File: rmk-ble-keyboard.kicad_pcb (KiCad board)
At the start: 2 copper layers, 285 x 94.5 mm, 124 parts, among them SW1 esc, SW10 9, SW11 0, SW12 -, SW13 =, SW14 backspace, SW15 tab, SW16 q, SW17 w, SW18 e, SW19 r, SW2 1, SW20 t, SW21 y, SW22 u, SW23 i, SW24 o, SW25 p, SW26 [, SW27 ], SW28 \, SW29 capslock, SW3 2, SW30 a, SW31 s, SW32 d, SW33 f, SW34 g, SW35 h, SW36 j, SW37 k, SW38 l, SW39 ;, SW4 3, SW40 ', SW41 enter, SW42 lshift, SW43 z, SW44 x, SW45 c, SW46 v, SW47 b, SW48 n, SW49 m, SW5 4, SW50 ,, SW51 ., SW52 /, SW53 rshift, SW54 lctrl, SW55 lgui, SW56 lalt, SW57 space, SW58 ralt, SW59 rgui, SW6 5, SW60 fn, SW61 rctrl, SW7 6, SW8 7, SW9 8, U2 USBLC6-2SC6

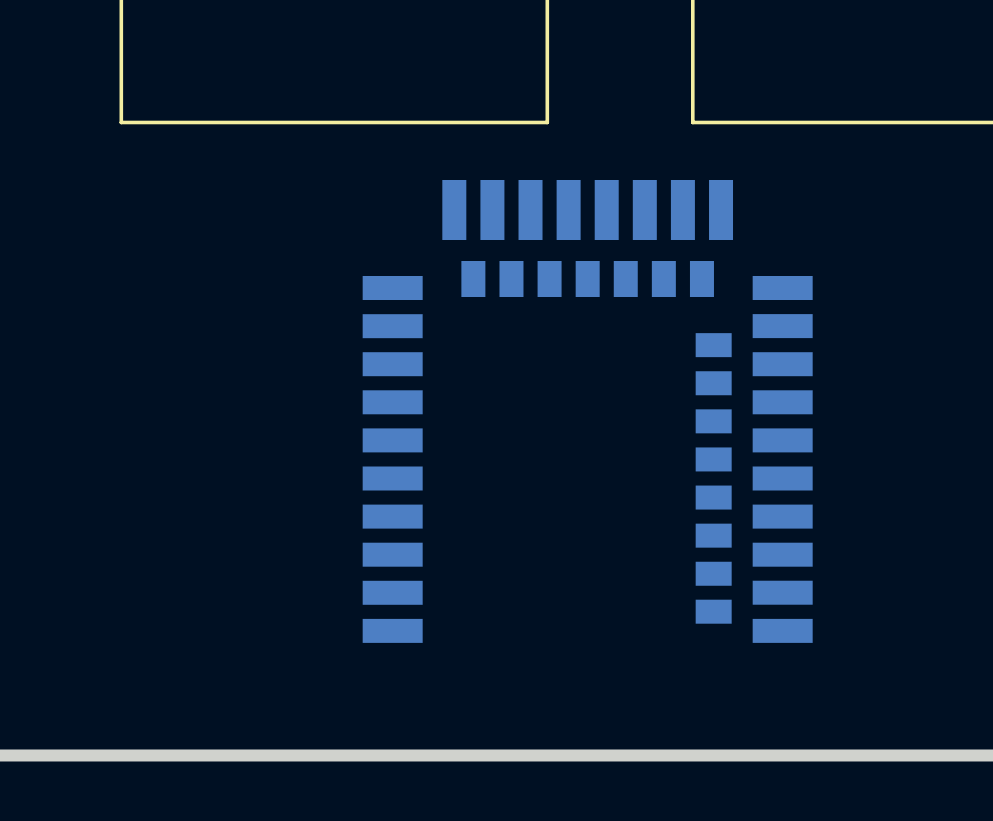
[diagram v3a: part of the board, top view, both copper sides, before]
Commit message: schema: rev0 done
Signed-off-by: HaoboGu <haobogu@outlook.com>
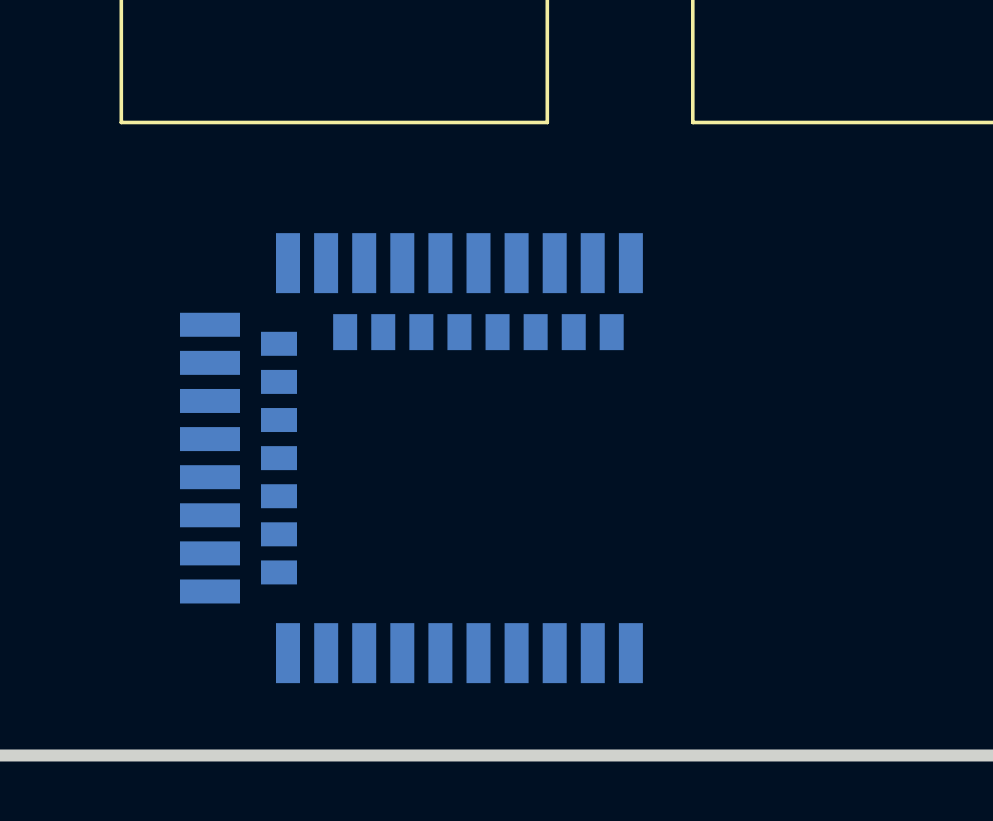
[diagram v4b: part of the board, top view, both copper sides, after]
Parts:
- moved U1 19.2 mm to (114.9, 107.0), turned to 0 degrees
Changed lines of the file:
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@@
 	(footprint "E73_2G4M08S1C:E73(2G4M08S1C)"
 		(layer "B.Cu")
-		(at 134.008 105.267 -90)
+		(at 114.919 107.038)
 		(property "Reference" "U1"
-			(at 8.525 14.7003 90)
+			(at 8.525 14.7003 180)
 			(unlocked yes)
 			(layer "B.SilkS")
@@
 		)
 		(property "Value" "~"
-			(at 8.525 -1.7003 90)
+			(at 8.525 -1.7003 180)
 			(unlocked yes)
 			(layer "B.Fab")
@@
 		)
 		(property "Footprint" "E73_2G4M08S1C:E73(2G4M08S1C)"
-			(at 0 0 90)
+			(at 0 0 180)
 			(unlocked yes)
 			(layer "B.Fab")
@@
 		)
 		(property "Datasheet" ""
-			(at 0 0 90)
+			(at 0 0 180)
 			(unlocked yes)
 			(layer "B.Fab")
@@
 		)
 		(property "Description" ""
-			(at 0 0 90)
+			(at 0 0 180)
 			(unlocked yes)
 			(layer "B.Fab")
@@
 		)
 		(fp_line
+			(start 18 0)
+			(end 0 0)
+			(stroke
+				(width 0.1)
+				(type solid)
+			)
+			(layer "B.SilkS")
+		)
+		(fp_line
 			(start 18 13)
 			(end 0 13)
@@
 			(layer "B.SilkS")
 		)
-		(fp_line
-			(start 18 0)
-			(end 0 0)
-			(stroke
-				(width 0.1)
-				(type solid)
-			)
-			(layer "B.SilkS")
-		)
 		(pad "1" smd rect
-			(at 14.03 13)
+			(at 14.03 13 90)
 			(size 2 0.8)
 			(layers "B.Cu" "B.Paste" "B.Mask")
@@
 		)
 		(pad "2" smd rect
-			(at 12.76 13)
+			(at 12.76 13 90)
 			(size 2 0.8)
 			(layers "B.Cu" "B.Paste" "B.Mask")
@@
 		)
 		(pad "3" smd rect
-			(at 11.49 13)
+			(at 11.49 13 90)
 			(size 2 0.8)
 			(layers "B.Cu" "B.Paste" "B.Mask")
@@
 		)
 		(pad "4" smd rect
-			(at 10.22 13)
+			(at 10.22 13 90)
 			(size 2 0.8)
 			(layers "B.Cu" "B.Paste" "B.Mask")
@@
 		)
 		(pad "5" smd rect
-			(at 8.95 13)
+			(at 8.95 13 90)
 			(size 2 0.8)
 			(layers "B.Cu" "B.Paste" "B.Mask")
@@
 		)
 		(pad "6" smd rect
-			(at 7.68 13)
+			(at 7.68 13 90)
 			(size 2 0.8)
 			(layers "B.Cu" "B.Paste" "B.Mask")
@@
 		)
 		(pad "7" smd rect
-			(at 6.41 13)
+			(at 6.41 13 90)
 			(size 2 0.8)
 			(layers "B.Cu" "B.Paste" "B.Mask")
@@
 		)
 		(pad "8" smd rect
-			(at 5.14 13)
+			(at 5.14 13 90)
 			(size 2 0.8)
 			(layers "B.Cu" "B.Paste" "B.Mask")
@@
 		)
 		(pad "9" smd rect
-			(at 3.8728 13.0003)
+			(at 3.8728 13.0003 90)
 			(size 2 0.8)
 			(layers "B.Cu" "B.Paste" "B.Mask")
@@
 		)
 		(pad "10" smd rect
-			(at 2.6 13)
+			(at 2.6 13 90)
 			(size 2 0.8)
 			(layers "B.Cu" "B.Paste" "B.Mask")
@@
 		)
 		(pad "11" smd rect
-			(at 0 10.945 270)
+			(at 0 10.945)
 			(size 2 0.8)
 			(layers "B.Cu" "B.Paste" "B.Mask")
@@
 		)
 		(pad "12" smd rect
-			(at 2.3 10.30975 270)
+			(at 2.3 10.30975)
 			(size 1.2 0.8)
 			(layers "B.Cu" "B.Paste" "B.Mask")
@@
 		)
 		(pad "13" smd rect
-			(at 0 9.675 270)
+			(at 0 9.675)
 			(size 2 0.8)
 			(layers "B.Cu" "B.Paste" "B.Mask")
@@
 		)
 		(pad "14" smd rect
-			(at 2.3 9.03975 270)
+			(at 2.3 9.03975)
 			(size 1.2 0.8)
 			(layers "B.Cu" "B.Paste" "B.Mask")
@@
 		)
 		(pad "15" smd rect
-			(at 0 8.405 270)
+			(at 0 8.405)
 			(size 2 0.8)
 			(layers "B.Cu" "B.Paste" "B.Mask")
@@
 		)
 		(pad "16" smd rect
-			(at 2.3 7.76975 270)
+			(at 2.3 7.76975)
 			(size 1.2 0.8)
 			(layers "B.Cu" "B.Paste" "B.Mask")
@@
 		)
 		(pad "17" smd rect
-			(at 0 7.135 270)
+			(at 0 7.135)
 			(size 2 0.8)
 			(layers "B.Cu" "B.Paste" "B.Mask")
@@
 		)
 		(pad "18" smd rect
-			(at 2.3 6.49975 270)
+			(at 2.3 6.49975)
 			(size 1.2 0.8)
 			(layers "B.Cu" "B.Paste" "B.Mask")
@@
 		)
 		(pad "19" smd rect
-			(at 0 5.865 270)
+			(at 0 5.865)
 			(size 2 0.8)
 			(layers "B.Cu" "B.Paste" "B.Mask")
@@
 		)
 		(pad "20" smd rect
-			(at 2.3 5.22975 270)
+			(at 2.3 5.22975)
 			(size 1.2 0.8)
 			(layers "B.Cu" "B.Paste" "B.Mask")
@@
 		)
 		(pad "21" smd rect
-			(at 0 4.595 270)
+			(at 0 4.595)
 			(size 2 0.8)
 			(layers "B.Cu" "B.Paste" "B.Mask")
@@
 		)
 		(pad "22" smd rect
-			(at 2.3 3.95975 270)
+			(at 2.3 3.95975)
 			(size 1.2 0.8)
 			(layers "B.Cu" "B.Paste" "B.Mask")
@@
 		)
 		(pad "23" smd rect
-			(at 0 3.325 270)
+			(at 0 3.325)
 			(size 2 0.8)
 			(layers "B.Cu" "B.Paste" "B.Mask")
@@
 		)
 		(pad "24" smd rect
-			(at 2.3 2.69 270)
+			(at 2.3 2.69)
 			(size 1.2 0.8)
 			(layers "B.Cu" "B.Paste" "B.Mask")
@@
 		)
 		(pad "25" smd rect
-			(at 0 2.055 270)
+			(at 0 2.055)
 			(size 2 0.8)
 			(layers "B.Cu" "B.Paste" "B.Mask")
@@
 		)
 		(pad "26" smd rect
-			(at 2.6 0 180)
+			(at 2.6 0 270)
 			(size 2 0.8)
 			(layers "B.Cu" "B.Paste" "B.Mask")
@@
 		)
 		(pad "27" smd rect
-			(at 3.87 0 180)
+			(at 3.87 0 270)
 			(size 2 0.8)
 			(layers "B.Cu" "B.Paste" "B.Mask")
@@
 		)
 		(pad "28" smd rect
-			(at 4.505 2.3)
+			(at 4.505 2.3 90)
 			(size 1.2 0.8)
 			(layers "B.Cu" "B.Paste" "B.Mask")
@@
 		)
 		(pad "29" smd rect
-			(at 5.14 0 180)
+			(at 5.14 0 270)
 			(size 2 0.8)
 			(layers "B.Cu" "B.Paste" "B.Mask")
@@
 		)
 		(pad "30" smd rect
-			(at 5.775 2.3)
+			(at 5.775 2.3 90)
 			(size 1.2 0.8)
 			(layers "B.Cu" "B.Paste" "B.Mask")
@@
 		)
 		(pad "31" smd rect
-			(at 6.41 0 180)
+			(at 6.41 0 270)
 			(size 2 0.8)
 			(layers "B.Cu" "B.Paste" "B.Mask")
@@
 		)
 		(pad "32" smd rect
-			(at 7.045 2.3)
+			(at 7.045 2.3 90)
 			(size 1.2 0.8)
 			(layers "B.Cu" "B.Paste" "B.Mask")
@@
 		)
 		(pad "33" smd rect
-			(at 7.68 0 180)
+			(at 7.68 0 270)
 			(size 2 0.8)
 			(layers "B.Cu" "B.Paste" "B.Mask")
@@
 		)
 		(pad "34" smd rect
-			(at 8.315 2.3)
+			(at 8.315 2.3 90)
 			(size 1.2 0.8)
 			(layers "B.Cu" "B.Paste" "B.Mask")
@@
 		)
 		(pad "35" smd rect
-			(at 8.95 0 180)
+			(at 8.95 0 270)
 			(size 2 0.8)
 			(layers "B.Cu" "B.Paste" "B.Mask")
@@
 		)
 		(pad "36" smd rect
-			(at 9.585 2.3)
+			(at 9.585 2.3 90)
 			(size 1.2 0.8)
 			(layers "B.Cu" "B.Paste" "B.Mask")
@@
 		)
 		(pad "37" smd rect
-			(at 10.22 0 180)
+			(at 10.22 0 270)
 			(size 2 0.8)
 			(layers "B.Cu" "B.Paste" "B.Mask")
@@
 		)
 		(pad "38" smd rect
-			(at 10.855 2.3)
+			(at 10.855 2.3 90)
 			(size 1.2 0.8)
 			(layers "B.Cu" "B.Paste" "B.Mask")
@@
 		)
 		(pad "39" smd rect
-			(at 11.49 0 180)
+			(at 11.49 0 270)
 			(size 2 0.8)
 			(layers "B.Cu" "B.Paste" "B.Mask")
@@
 		)
 		(pad "40" smd rect
-			(at 12.125 2.3)
+			(at 12.125 2.3 90)
 			(size 1.2 0.8)
 			(layers "B.Cu" "B.Paste" "B.Mask")
@@
 		)
 		(pad "41" smd rect
-			(at 12.7572 -0.0003 180)
+			(at 12.7572 -0.0003 270)
 			(size 2 0.8)
 			(layers "B.Cu" "B.Paste" "B.Mask")
@@
 		)
 		(pad "42" smd rect
-			(at 13.39 2.3)
+			(at 13.39 2.3 90)
 			(size 1.2 0.8)
 			(layers "B.Cu" "B.Paste" "B.Mask")
@@
 		)
 		(pad "43" smd rect
-			(at 14.03 0 180)
-			(size 2 0.8)
-			(layers "B.Cu" "B.Paste" "B.Mask")
+			(at 14.03 0 270)
+			(size 2 0.8)
+			(layers "B.Cu" "B.Paste" "B.Mask")

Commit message: assign footprints
Signed-off-by: HaoboGu <haobogu@outlook.com>
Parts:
- added C1: 10uf, Capacitor_SMD:C_0603_1608Metric_Pad1.08x0.95mm_HandSolder, F.Cu at (136.9, 147.4)
- added C2: 10uf, Capacitor_SMD:C_0603_1608Metric_Pad1.08x0.95mm_HandSolder, F.Cu at (136.9, 149.9)
- added C3: 1uf, Capacitor_SMD:C_0603_1608Metric_Pad1.08x0.95mm_HandSolder, F.Cu at (136.9, 152.4)
- added C4: 1uf, Capacitor_SMD:C_0603_1608Metric_Pad1.08x0.95mm_HandSolder, F.Cu at (136.9, 154.9)
- added D62: LED, LED_SMD:LED_0603_1608Metric_Pad1.05x0.95mm_HandSolder, F.Cu at (170.8, 144.1)
- added D63: B5819W, B5819W-SL:SOD-123_L2.7-W1.6-LS3.7-RD-1, F.Cu at (153.2, 160.0)
- added D64: LED, LED_SMD:LED_0603_1608Metric_Pad1.05x0.95mm_HandSolder, F.Cu at (170.8, 146.7)
- added J1: USB_C_Receptacle_USB2.0_16P, Connector_USB:USB_C_Receptacle_GCT_USB4105-xx-A_16P_TopMnt_Horizontal, F.Cu at (140.5, 141.4)
- added J2: Battery, Connector_JST:JST_SH_SM02B-SRSS-TB_1x02-1MP_P1.00mm_Horizontal, F.Cu at (153.8, 149.9)
- added J3: Debug, Connector_PinHeader_2.54mm:PinHeader_1x04_P2.54mm_Vertical, F.Cu at (161.6, 138.5)
- added J4: RGB, Connector_PinHeader_2.54mm:PinHeader_1x03_P2.54mm_Vertical, F.Cu at (166.2, 138.5)
- added J5: Reset, Connector_PinHeader_2.54mm:PinHeader_1x02_P2.54mm_Vertical, F.Cu at (166.2, 148.2)
- added Q1: Si2301CDS, Package_TO_SOT_SMD:SOT-23-5_HandSoldering, F.Cu at (153.3, 156.2)
- added R1: 5.1K, Resistor_SMD:R_0603_1608Metric_Pad0.98x0.95mm_HandSolder, F.Cu at (136.9, 157.4)
- added R10: 1K, Resistor_SMD:R_0603_1608Metric_Pad0.98x0.95mm_HandSolder, F.Cu at (175.1, 146.6)
- added R2: 5.1K, Resistor_SMD:R_0603_1608Metric_Pad0.98x0.95mm_HandSolder, F.Cu at (136.9, 159.9)
- added R3: 3K, Resistor_SMD:R_0603_1608Metric_Pad0.98x0.95mm_HandSolder, F.Cu at (141.2, 147.4)
- added R4: 0.4, Resistor_SMD:R_0805_2012Metric_Pad1.20x1.40mm_HandSolder, F.Cu at (145.8, 160.2)
- added R5: 10K, Resistor_SMD:R_0603_1608Metric_Pad0.98x0.95mm_HandSolder, F.Cu at (141.2, 149.9)
- added R6: 1K, Resistor_SMD:R_0603_1608Metric_Pad0.98x0.95mm_HandSolder, F.Cu at (175.1, 144.0)
- added R7: 100K, Resistor_SMD:R_0603_1608Metric_Pad0.98x0.95mm_HandSolder, F.Cu at (141.2, 152.4)
- added R8: 810K, Resistor_SMD:R_0603_1608Metric_Pad0.98x0.95mm_HandSolder, F.Cu at (141.2, 154.9)
- added R9: 2M, Resistor_SMD:R_0603_1608Metric_Pad0.98x0.95mm_HandSolder, F.Cu at (141.2, 157.4)
- added SW62: MSK-12C02, MSK-12C02:SW-TH_MSK12C02, F.Cu at (151.1, 139.1)
- added SW63: key, Button_Switch_SMD:SW_Push_1P1T_XKB_TS-1187A, F.Cu at (172.5, 137.4)
- added U3: TP4056, TP4056:ESOP-8_L4.9-W3.9-P1.27-LS6.0-BL-EP, F.Cu at (147.2, 150.1)
- added U5: AP2112K-3.3, Package_TO_SOT_SMD:SOT-23-5, F.Cu at (146.0, 156.5)
- added Y1: 32.768KHZ, Crystal:Crystal_SMD_3215-2Pin_3.2x1.5mm, F.Cu at (171.1, 149.6)
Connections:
- D1 pad 1: row1 -> /matrix/row1
- D10 pad 1: row1 -> /matrix/row1
- D11 pad 1: row1 -> /matrix/row1
- D12 pad 1: row1 -> /matrix/row1
- D13 pad 1: row1 -> /matrix/row1
- D14 pad 1: row1 -> /matrix/row1
- D15 pad 1: row2 -> /matrix/row2
- D16 pad 1: row2 -> /matrix/row2
- D17 pad 1: row2 -> /matrix/row2
- D18 pad 1: row2 -> /matrix/row2
- D19 pad 1: row2 -> /matrix/row2
- D2 pad 1: row1 -> /matrix/row1
- D20 pad 1: row2 -> /matrix/row2
- D21 pad 1: row2 -> /matrix/row2
- D22 pad 1: row2 -> /matrix/row2
- D23 pad 1: row2 -> /matrix/row2
- D24 pad 1: row2 -> /matrix/row2
- D25 pad 1: row2 -> /matrix/row2
- D26 pad 1: row2 -> /matrix/row2
- D27 pad 1: row2 -> /matrix/row2
- D28 pad 1: row2 -> /matrix/row2
- D29 pad 1: row3 -> /matrix/row3
- D3 pad 1: row1 -> /matrix/row1
- D30 pad 1: row3 -> /matrix/row3
- D31 pad 1: row3 -> /matrix/row3
- D32 pad 1: row3 -> /matrix/row3
- D33 pad 1: row3 -> /matrix/row3
- D34 pad 1: row3 -> /matrix/row3
- D35 pad 1: row3 -> /matrix/row3
- D36 pad 1: row3 -> /matrix/row3
- D37 pad 1: row3 -> /matrix/row3
- D38 pad 1: row3 -> /matrix/row3
- D39 pad 1: row3 -> /matrix/row3
- D4 pad 1: row1 -> /matrix/row1
- D40 pad 1: row3 -> /matrix/row3
- D41 pad 1: row4 -> /matrix/row4
- D42 pad 1: row3 -> /matrix/row3
- D43 pad 1: row4 -> /matrix/row4
- D44 pad 1: row4 -> /matrix/row4
- D45 pad 1: row4 -> /matrix/row4
- D46 pad 1: row4 -> /matrix/row4
- D47 pad 1: row4 -> /matrix/row4
- D48 pad 1: row4 -> /matrix/row4
- D49 pad 1: row4 -> /matrix/row4
- D5 pad 1: row1 -> /matrix/row1
- D50 pad 1: row4 -> /matrix/row4
- D51 pad 1: row4 -> /matrix/row4
- D52 pad 1: row4 -> /matrix/row4
- D53 pad 1: row4 -> /matrix/row4
- D54 pad 1: row5 -> /matrix/row5
- D55 pad 1: row5 -> /matrix/row5
- D56 pad 1: row5 -> /matrix/row5
- D57 pad 1: row5 -> /matrix/row5
- D58 pad 1: row5 -> /matrix/row5
- D59 pad 1: row5 -> /matrix/row5
- D6 pad 1: row1 -> /matrix/row1
- D60 pad 1: row5 -> /matrix/row5
- D61 pad 1: row5 -> /matrix/row5
- D7 pad 1: row1 -> /matrix/row1
- D8 pad 1: row1 -> /matrix/row1
- D9 pad 1: row1 -> /matrix/row1
- SW1 pad 1: col1 -> /matrix/col1
- SW10 pad 1: col10 -> /matrix/col10
- SW11 pad 1: col11 -> /matrix/col11
- SW12 pad 1: col12 -> /matrix/col12
- SW13 pad 1: col13 -> /matrix/col13
- SW14 pad 1: col14 -> /matrix/col14
- SW15 pad 1: col1 -> /matrix/col1
- SW16 pad 1: col2 -> /matrix/col2
- SW17 pad 1: col3 -> /matrix/col3
- SW18 pad 1: col4 -> /matrix/col4
- SW19 pad 1: col5 -> /matrix/col5
- SW2 pad 1: col2 -> /matrix/col2
- SW20 pad 1: col6 -> /matrix/col6
- SW21 pad 1: col7 -> /matrix/col7
- SW22 pad 1: col8 -> /matrix/col8
- SW23 pad 1: col9 -> /matrix/col9
- SW24 pad 1: col10 -> /matrix/col10
- SW25 pad 1: col11 -> /matrix/col11
- SW26 pad 1: col12 -> /matrix/col12
- SW27 pad 1: col13 -> /matrix/col13
- SW28 pad 1: col14 -> /matrix/col14
- SW29 pad 1: col1 -> /matrix/col1
- SW3 pad 1: col3 -> /matrix/col3
- SW30 pad 1: col2 -> /matrix/col2
- SW31 pad 1: col3 -> /matrix/col3
- SW32 pad 1: col4 -> /matrix/col4
- SW33 pad 1: col5 -> /matrix/col5
- SW34 pad 1: col6 -> /matrix/col6
- SW35 pad 1: col7 -> /matrix/col7
- SW36 pad 1: col8 -> /matrix/col8
- SW37 pad 1: col9 -> /matrix/col9
- SW38 pad 1: col10 -> /matrix/col10
- SW39 pad 1: col11 -> /matrix/col11
- SW4 pad 1: col4 -> /matrix/col4
- SW40 pad 1: col12 -> /matrix/col12
- SW41 pad 1: col14 -> /matrix/col14
- SW42 pad 1: col1 -> /matrix/col1
- SW43 pad 1: col2 -> /matrix/col2
- SW44 pad 1: col3 -> /matrix/col3
- SW45 pad 1: col4 -> /matrix/col4
- SW46 pad 1: col5 -> /matrix/col5
- SW47 pad 1: col6 -> /matrix/col6
- SW48 pad 1: col7 -> /matrix/col7
- SW49 pad 1: col8 -> /matrix/col8
- SW5 pad 1: col5 -> /matrix/col5
- SW50 pad 1: col9 -> /matrix/col9
- SW51 pad 1: col10 -> /matrix/col10
- SW52 pad 1: col11 -> /matrix/col11
- SW53 pad 1: col14 -> /matrix/col14
- SW54 pad 1: col1 -> /matrix/col1
- SW55 pad 1: col2 -> /matrix/col2
- SW56 pad 1: col3 -> /matrix/col3
- SW57 pad 1: col6 -> /matrix/col6
- SW58 pad 1: col10 -> /matrix/col10
- SW59 pad 1: col11 -> /matrix/col11
- SW6 pad 1: col6 -> /matrix/col6
- SW60 pad 1: col13 -> /matrix/col13
- SW61 pad 1: col14 -> /matrix/col14
- SW7 pad 1: col7 -> /matrix/col7
- SW8 pad 1: col8 -> /matrix/col8
- SW9 pad 1: col9 -> /matrix/col9
- U1 pad 1: unconnected-(U1-P1.11-Pad1) -> /matrix/col4
- U1 pad 10: unconnected-(U1-AI6-Pad10) -> /matrix/row5
- U1 pad 11: unconnected-(U1-XL1-Pad11) -> Net-(U1-XL1)
- U1 pad 13: unconnected-(U1-XL2-Pad13) -> Net-(U1-XL2)
- U1 pad 15: unconnected-(U1-AI3-Pad15) -> /matrix/col5
- U1 pad 16: unconnected-(U1-P0.08-Pad16) -> /mcu/charging_led
- U1 pad 17: unconnected-(U1-P1.09-Pad17) -> /matrix/col6
- U1 pad 18: unconnected-(U1-AI2-Pad18) -> /mcu/bat_adc
- U1 pad 19: unconnected-(U1-VCC-Pad19) -> 3V3
- U1 pad 2: unconnected-(U1-P1.10-Pad2) -> /matrix/col3
- U1 pad 21: unconnected-(U1-GND-Pad21) -> GND
- U1 pad 23: unconnected-(U1-VDH-Pad23) -> 3V3
- U1 pad 24: unconnected-(U1-GND-Pad24) -> GND
- U1 pad 26: unconnected-(U1-RST-Pad26) -> Net-(J5-Pin_1)
- U1 pad 27: unconnected-(U1-VBS-Pad27) -> VBUS
- U1 pad 28: unconnected-(U1-P15-Pad28) -> /matrix/col11
- U1 pad 29: unconnected-(U1-D--Pad29) -> /mcu/D-
- U1 pad 3: unconnected-(U1-P0.03-Pad3) -> /matrix/col2
- U1 pad 30: unconnected-(U1-P17-Pad30) -> /matrix/col12
- U1 pad 31: unconnected-(U1-D+-Pad31) -> /mcu/D+
- U1 pad 32: unconnected-(U1-P0.20-Pad32) -> /matrix/col13
- U1 pad 33: unconnected-(U1-P0.13-Pad33) -> /matrix/col7
- U1 pad 34: unconnected-(U1-P0.22-Pad34) -> /matrix/col14
- U1 pad 35: unconnected-(U1-P0.24-Pad35) -> /matrix/col8
- U1 pad 36: unconnected-(U1-P1.00-Pad36) -> Net-(U1-P1.00)
- U1 pad 37: unconnected-(U1-SWD-Pad37) -> /mcu/swd
- U1 pad 38: unconnected-(U1-P1.02-Pad38) -> /mcu/rgb
- U1 pad 39: unconnected-(U1-SWC-Pad39) -> /mcu/swc
- U1 pad 4: unconnected-(U1-AI4-Pad4) -> /matrix/col1
- U1 pad 40: unconnected-(U1-P1.04-Pad40) -> /mcu/CHARGE
- U1 pad 41: unconnected-(U1-NF1-Pad41) -> /matrix/col9
- U1 pad 42: unconnected-(U1-P1.06-Pad42) -> /mcu/caps
- U1 pad 43: unconnected-(U1-NF2-Pad43) -> /matrix/col10
- U1 pad 5: unconnected-(U1-GND-Pad5) -> GND
- U1 pad 6: unconnected-(U1-P1.13-Pad6) -> /matrix/row1
- U1 pad 7: unconnected-(U1-AI0-Pad7) -> /matrix/row2
- U1 pad 8: unconnected-(U1-AI5-Pad8) -> /matrix/row3
- U1 pad 9: unconnected-(U1-AI7-Pad9) -> /matrix/row4
- U2 pad 1: unconnected-(U2-I/O1-Pad1) -> /power/DP
- U2 pad 2: unconnected-(U2-GND-Pad2) -> GND
- U2 pad 3: unconnected-(U2-I/O2-Pad3) -> /power/DN
- U2 pad 4: unconnected-(U2-I/O2-Pad4) -> /mcu/D-
- U2 pad 5: unconnected-(U2-VBUS-Pad5) -> VBUS
- U2 pad 6: unconnected-(U2-I/O1-Pad6) -> /mcu/D+
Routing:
- net row4: track 242.2 -> 0.00 mm
- net /matrix/row4: track 0.00 -> 242.2 mm
- net col2: track 89.9 -> 0.00 mm
- net /matrix/col2: track 0.00 -> 89.9 mm
- net col3: track 87.4 -> 0.00 mm
- net /matrix/col3: track 0.00 -> 87.4 mm
- net col14: track 85.9 -> 0.00 mm
- net /matrix/col14: track 0.00 -> 85.9 mm
- net col6: track 83.7 -> 0.00 mm
- net col11: track 83.7 -> 0.00 mm
- net col10: track 83.7 -> 0.00 mm
- net /matrix/col6: track 0.00 -> 83.7 mm
- net /matrix/col11: track 0.00 -> 83.7 mm
- net /matrix/col10: track 0.00 -> 83.7 mm
- net col1: track 82.4 -> 0.00 mm
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
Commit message: add hole footprint from gh60, update pcb
Signed-off-by: HaoboGu <haobogu@outlook.com>
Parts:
- added HOLE: VAL**, hole:PKRHSL, F.Cu at (32.0, 88.9)
- added HOLE: VAL**, hole:PKRHSL, F.Cu at (313.7, 88.4)
- added HOLE: VAL**, hole:PKRH, F.Cu at (157.5, 75.4)
- added HOLE: VAL**, hole:PKRHC, F.Cu at (54.9, 53.1)
- added HOLE: VAL**, hole:PKRH, F.Cu at (278.9, 45.0)
- J1: moved to B.Cu
- moved J1 144.2 mm to (47.5, 31.2)
- moved D1 6.20 mm to (35.0, 38.1), turned to -90 degrees
- moved D2 6.20 mm to (54.0, 38.1), turned to -90 degrees
- turned SW1 to 180 degrees
- turned SW2 to 180 degrees
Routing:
- net /matrix/col2: track 89.9 -> 82.4 mm
- net /matrix/col1: track 82.4 -> 76.8 mm

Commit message: update PCB config
Signed-off-by: HaoboGu <haobogu@outlook.com>
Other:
- outline, holes or cut-outs redrawn
- board text added: "PCB3D_BR_TEST"
- board text added: "PCB3D_TL_TEST"
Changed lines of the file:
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@@
 	)
 	(setup
+		(stackup
+			(layer "F.SilkS"
+				(type "Top Silk Screen")
+			)
+			(layer "F.Paste"
+				(type "Top Solder Paste")
+			)
+			(layer "F.Mask"
+				(type "Top Solder Mask")
+				(color "Green")
+				(thickness 0.01)
+			)
+			(layer "F.Cu"
+				(type "copper")
+				(thickness 0.035)
+			)
+			(layer "dielectric 1"
+				(type "core")
+				(thickness 1.51)
+				(material "FR4")
+				(epsilon_r 4.5)
+				(loss_tangent 0.02)
+			)
+			(layer "B.Cu"
+				(type "copper")
+				(thickness 0.035)
+			)
+			(layer "B.Mask"
+				(type "Bottom Solder Mask")
+				(color "Green")
+				(thickness 0.01)
+			)
+			(layer "B.Paste"
+				(type "Bottom Solder Paste")
+			)
+			(layer "B.SilkS"
+				(type "Bottom Silk Screen")
+			)
+			(copper_finish "None")
+			(dielectric_constraints no)
+		)
 		(pad_to_mask_clearance 0)
 		(allow_soldermask_bridges_in_footprints no)
+		(aux_axis_origin 28.956 123.444)
 		(pcbplotparams
 			(layerselection 0x00010fc_ffffffff)
@@
 	)
 	(gr_line
-		(start 313.95 28.95)
-		(end 313.95 123.45)
+		(start 313.95 30.95)
+		(end 313.95 121.45)
 		(stroke
 			(width 0.4)
@@
 	)
 	(gr_line
-		(start 28.95 123.45)
-		(end 28.95 28.95)
+		(start 28.95 121.45)
+		(end 28.95 30.95)
+		(stroke
+			(width 0.4)
+			(type default)
+		)
+		(layer "Edge.Cuts")
+	)
+	(gr_arc
+		(start 28.95 30.95)
+		(mid 29.535786 29.535786)
+		(end 30.95 28.95)
+		(stroke
+			(width 0.4)
+			(type default)
+		)
+		(layer "Edge.Cuts")
+	)
+	(gr_arc
+		(start 311.95 28.95)
+		(mid 313.364214 29.535786)
+		(end 313.95 30.95)
+		(stroke
+			(width 0.4)
+			(type default)
+		)
+		(layer "Edge.Cuts")
+	)
+	(gr_arc
+		(start 313.95 121.45)
+		(mid 313.364214 122.864214)
+		(end 311.95 123.45)
+		(stroke
+			(width 0.4)
+			(type default)
+		)
+		(layer "Edge.Cuts")
+	)
+	(gr_arc
+		(start 30.95 123.45)
+		(mid 29.535786 122.864214)
+		(end 28.95 121.45)
 		(stroke
 			(width 0.4)
@@
 	)
 	(gr_line
-		(start 28.95 28.95)
-		(end 313.95 28.95)
+		(start 30.95 28.95)
+		(end 311.95 28.95)
 		(stroke
 			(width 0.4)
@@
 	)
 	(gr_line
-		(start 313.95 123.45)
-		(end 28.95 123.45)
+		(start 311.95 123.45)
+		(end 30.95 123.45)
 		(stroke
 			(width 0.4)
@@
 		(layer "Edge.Cuts")
 	)
+	(gr_text "PCB3D_TL_TEST"
+		(at 28.956 28.956 0)
+		(layer "F.Cu")
+		(effects
+			(font
+				(size 1.5 1.5)
+				(thickness 0.3)
+				(bold yes)
+			)
+			(justify left bottom)
+		)
+	)
+	(gr_text "PCB3D_BR_TEST"
+		(at 313.944 123.444 0)
+		(layer "F.Cu")
+		(effects
+			(font
+				(size 1.5 1.5)
+				(thickness 0.3)
+				(bold yes)
+			)
+			(justify left bottom)
+		)
+	)
 	(segment
